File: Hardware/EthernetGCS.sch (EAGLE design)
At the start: 67 parts, among them IC3 24AA00OT, IC4 PIC24FJ64GA002_QFN, J2 HR911105A, Q2 25Mhz, U1 MIC5219-3.3V, U3 MIC5219-3.3V, U4 ENC28J60-QFN, U5 MIC5219-3.3V, U7 FT232RL-BASICSSOP, X2 USB-A-H

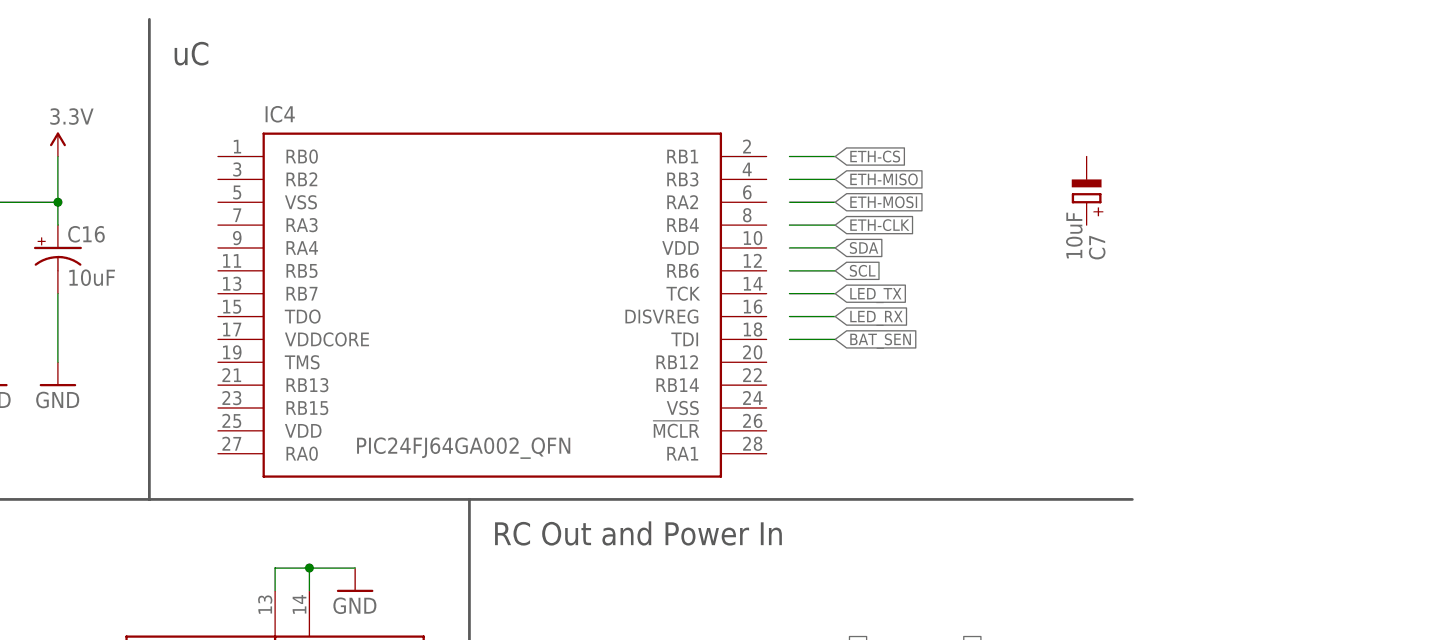
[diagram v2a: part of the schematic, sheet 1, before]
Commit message: Connecting the power pins of the uC.
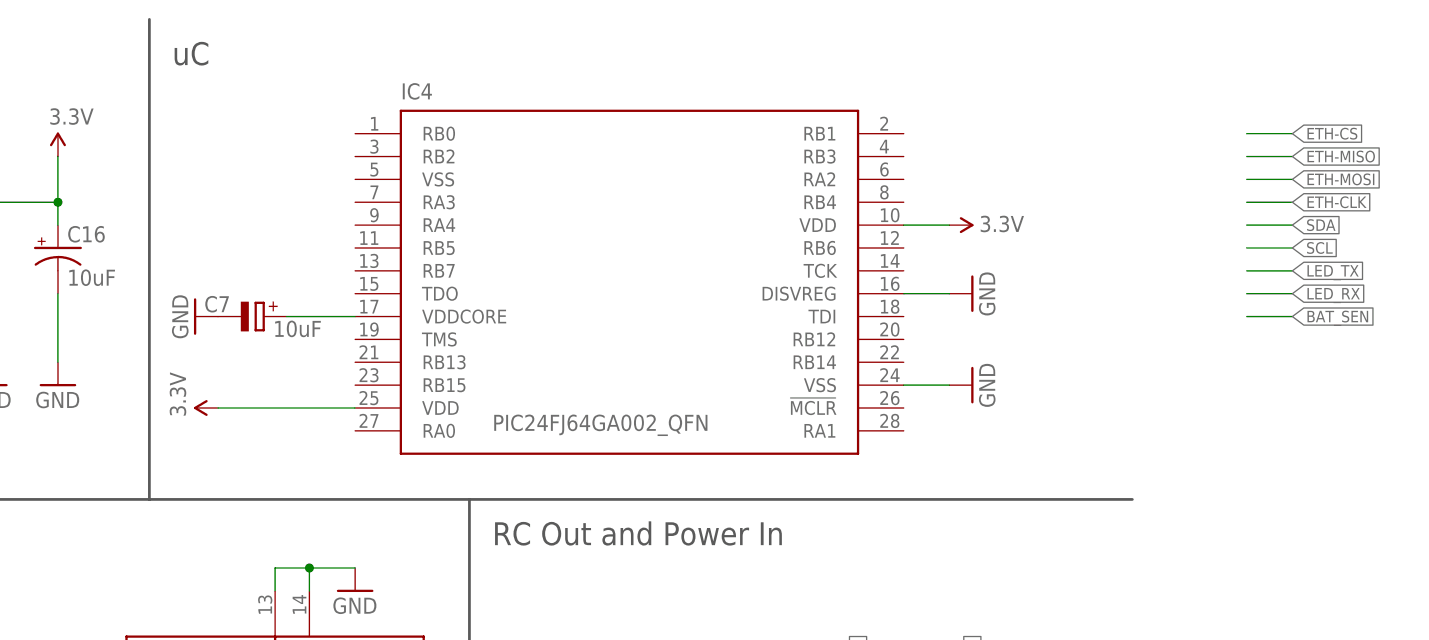
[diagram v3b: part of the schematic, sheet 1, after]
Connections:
- new net N$5: C7.+, IC4.VDDCORE
- net 3.3V: now also IC4.VDD@1, IC4.VDD@2
- net GND: now also C7.-, IC4.DISVREG, IC4.VSS@2
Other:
- moved on the sheet: C7, IC4

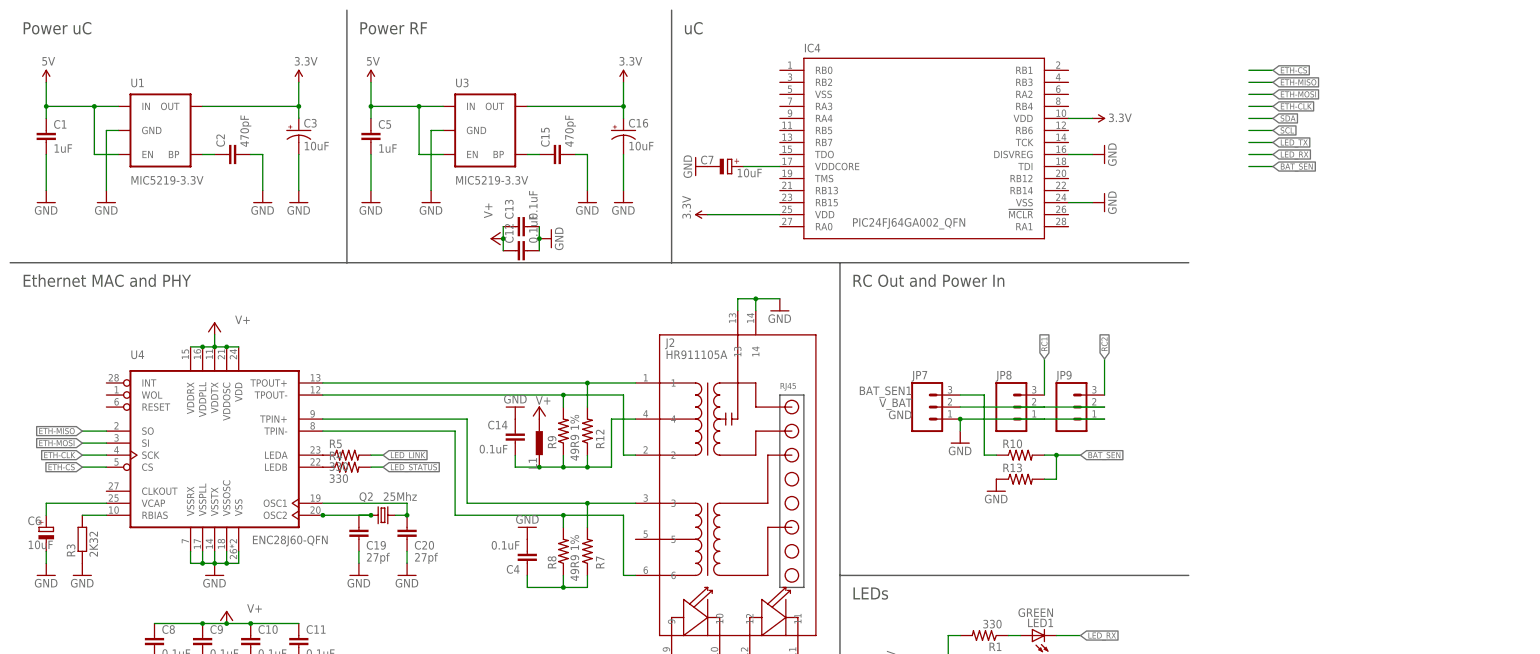
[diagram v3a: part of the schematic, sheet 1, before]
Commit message: Adding GPS port, RC output pull-ups. Connecting stuff, and changing parts positions.
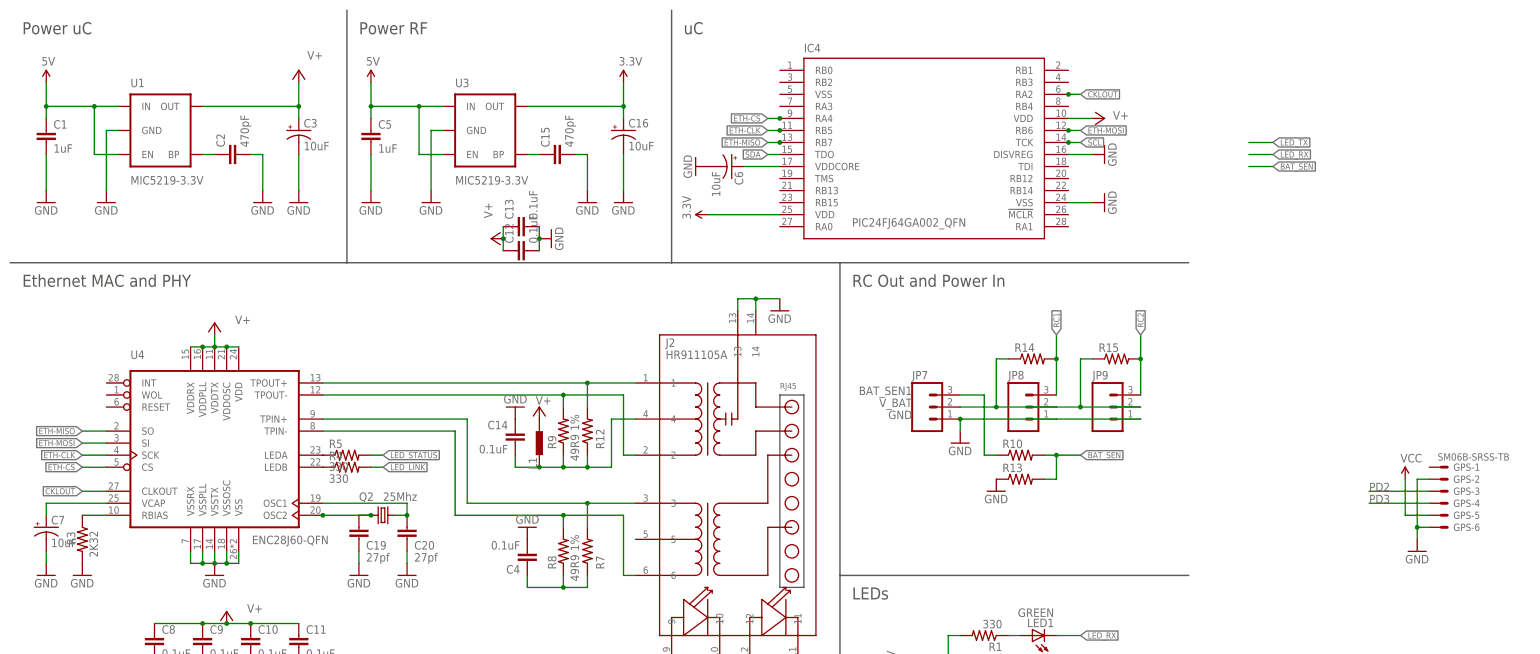
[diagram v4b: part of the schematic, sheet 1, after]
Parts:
- added GPS: SM06B-SRSS-TB, con-jst2:SM06B-SRSS-TB
- added R14, R15: (no value), SparkFun:RESISTOR0402-RES
- C6, C7: device rcl:CPOL-EUSMCA -> SparkFun:CAP_POL1206
- R3: device rcl:R-EU_R0805 -> SparkFun:RESISTOR0402-RES
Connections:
- new net CKLOUT: IC4.RA2, U4.CLKOUT
- new net PD2: GPS-3.S
- new net PD3: GPS-4.S
- new net VCC: GPS-5.S
- net 3.3V: no longer C3.+, IC4.VDD@1, U1.OUT
- net ETH-CLK: now also IC4.RB5
- net ETH-CS: now also IC4.RA4
- net ETH-MISO: now also IC4.RB7
- net ETH-MOSI: now also IC4.RB6
- net GND: now also GPS-2.S, GPS-6.S, R3.2; no longer R3.1
- net LED_LINK: now also R4.2; no longer R5.2
- net LED_STATUS: now also R5.2; no longer R4.2
- net N$13: now also C7.+; no longer C6.+
- net N$17: now also R3.1; no longer R3.2
- net N$5: now also C6.+; no longer C7.+
- net RC1: now also R14.2
- net RC2: now also R15.2
- net SCL: now also IC4.TCK
- net SDA: now also IC4.TDO
- net V+: now also C3.+, IC4.VDD@1, U1.OUT
- net V_BAT: now also R14.1, R15.1
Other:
- moved on the sheet: C6, C7, JP8, JP9

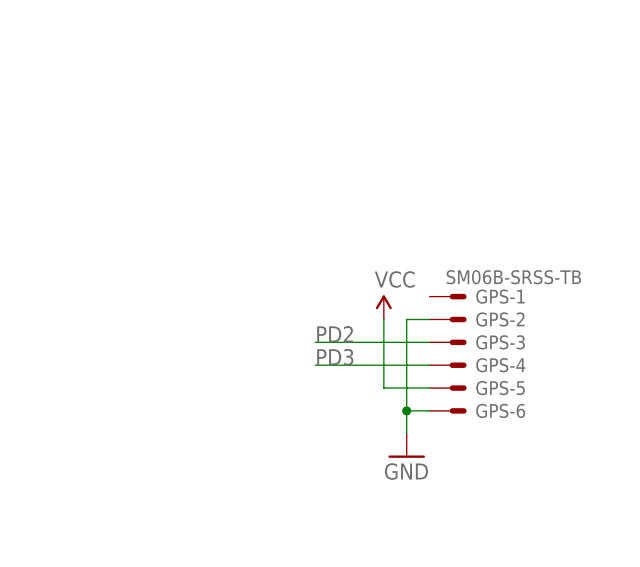
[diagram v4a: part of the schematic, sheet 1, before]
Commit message: Layout: tracing tracks.
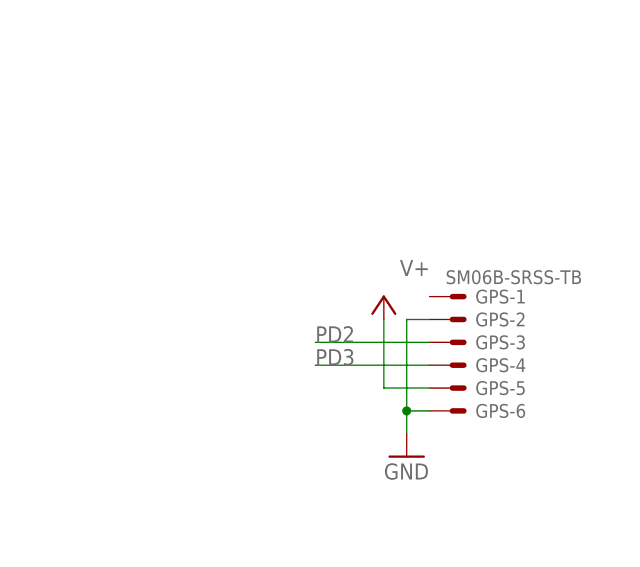
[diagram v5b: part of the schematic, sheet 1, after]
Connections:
- removed net VCC: GPS-5.S
- net V+: now also GPS-5.S
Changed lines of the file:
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@@
 <part name="GPS" library="con-jst2" deviceset="?M06B-SRSS-TB" device="S"/>
 <part name="GND44" library="supply1" deviceset="GND" device=""/>
-<part name="P+40" library="DIYdrones3" deviceset="VCC" device=""/>
+<part name="P+1" library="supply2" deviceset="V+" device=""/>
 </parts>
 <sheets>
@@
 <instance part="GPS" gate="-6" x="302.26" y="76.2"/>
 <instance part="GND44" gate="1" x="297.18" y="71.12"/>
-<instance part="P+40" gate="1" x="294.64" y="86.36"/>
+<instance part="P+1" gate="1" x="294.64" y="88.9" smashed="yes">
+<attribute name="VALUE" x="296.418" y="91.186" size="1.778" layer="96"/>
+</instance>
 </instances>
 <busses>
@@
 <pinref part="P+10" gate="1" pin="V+"/>
 </segment>
+<segment>
+<wire x1="299.72" y1="78.74" x2="294.64" y2="78.74" width="0.1524" layer="91"/>
+<wire x1="294.64" y1="78.74" x2="294.64" y2="86.36" width="0.1524" layer="91"/>
+<pinref part="GPS" gate="-5" pin="S"/>
+<pinref part="P+1" gate="1" pin="V+"/>
+</segment>
 </net>
 <net name="N$13" class="0">
@@
 </segment>
 </net>
-<net name="VCC" class="0">
-<segment>
-<wire x1="299.72" y1="78.74" x2="294.64" y2="78.74" width="0.1524" layer="91"/>
-<wire x1="294.64" y1="78.74" x2="294.64" y2="86.36" width="0.1524" layer="91"/>
-<pinref part="GPS" gate="-5" pin="S"/>
-<pinref part="P+40" gate="1" pin="VCC"/>
-</segment>
-</net>

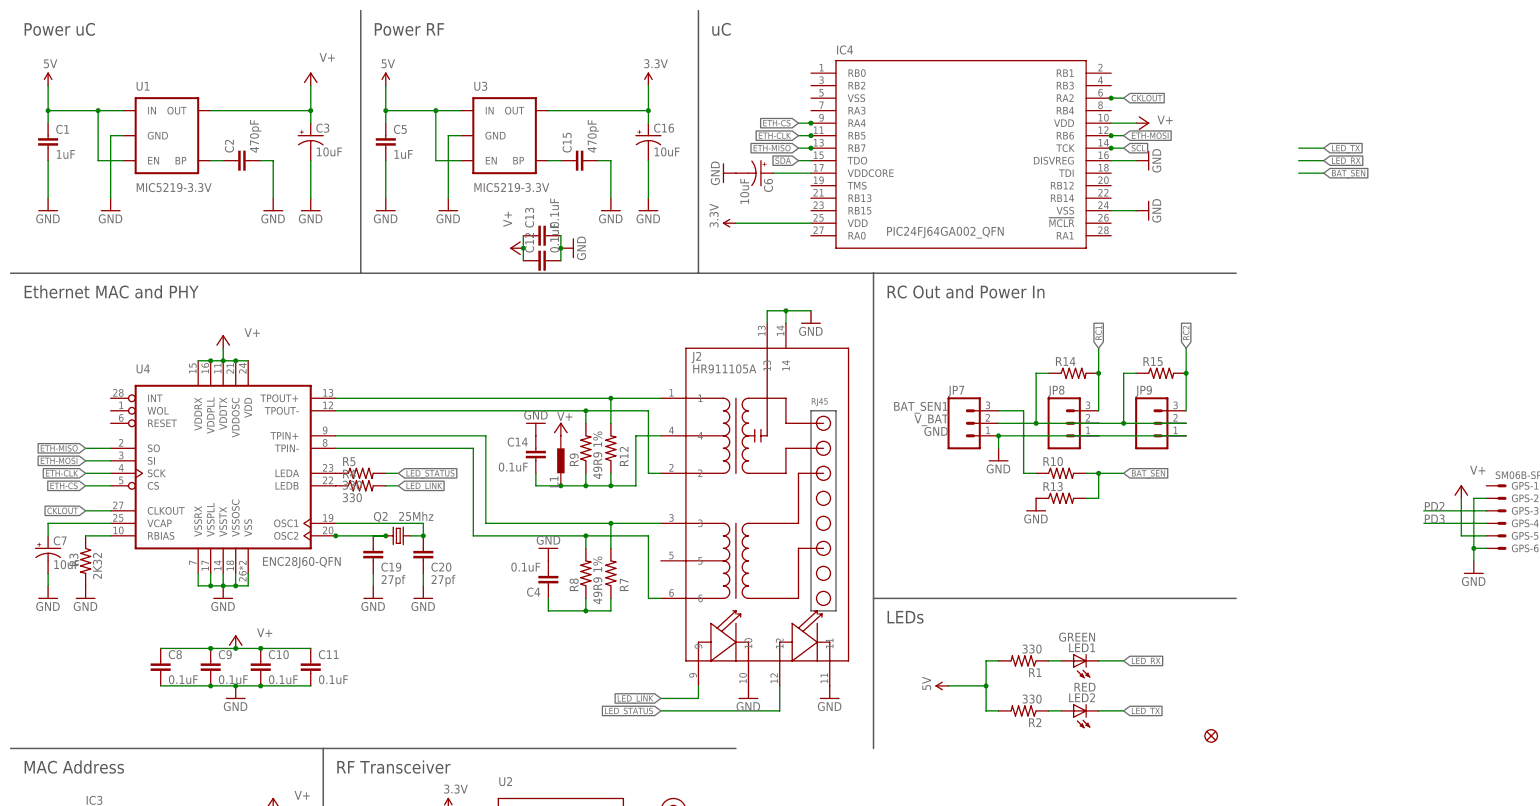
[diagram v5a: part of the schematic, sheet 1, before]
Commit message: Continuing the board layout, adding connections to the schematic
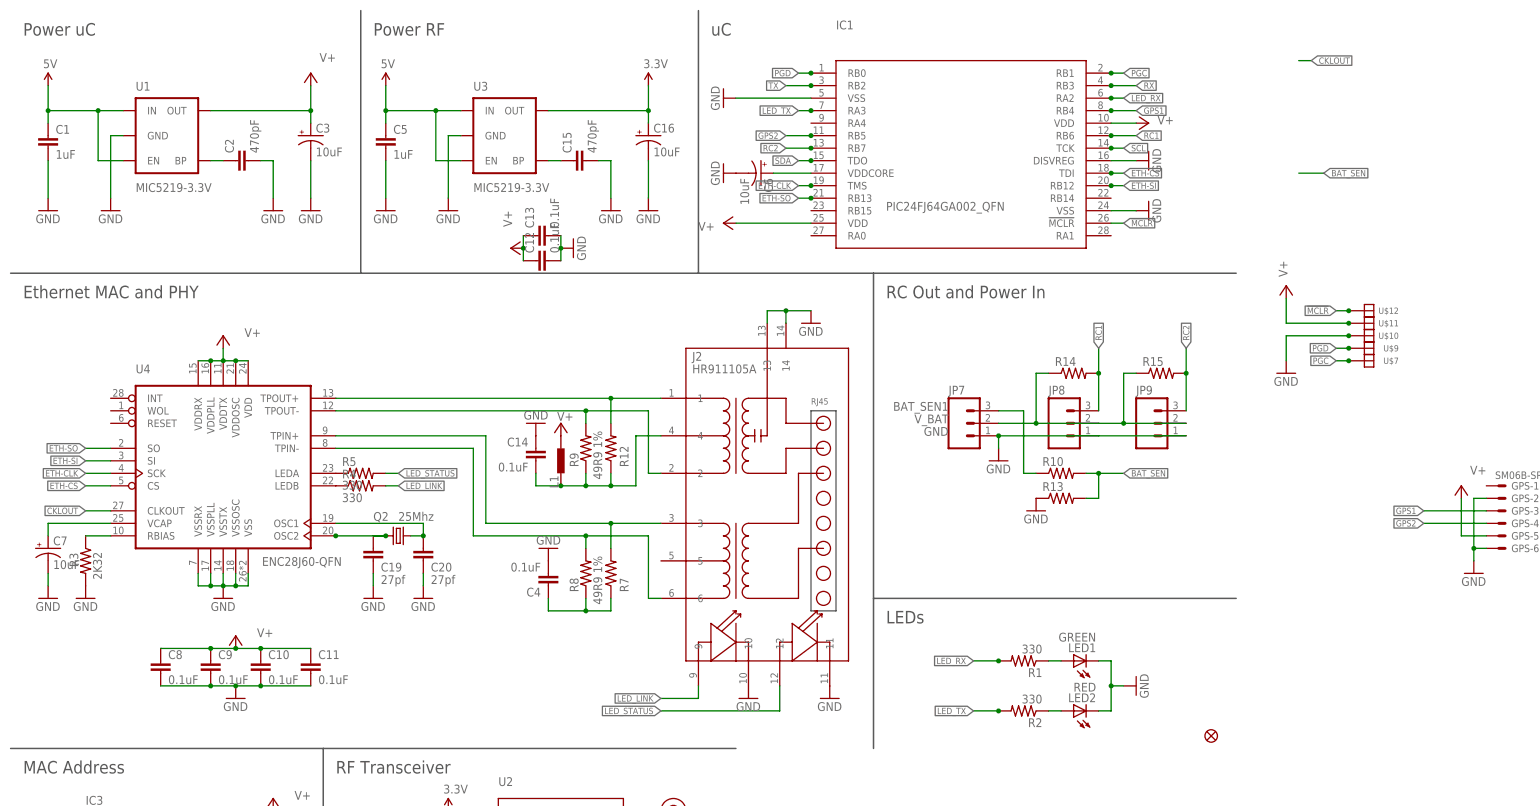
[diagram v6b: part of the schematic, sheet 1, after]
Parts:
- added U$10, U$11, U$12, U$7, U$9: SOLDER_PAD150_75, DIYdrones2:SOLDER_PAD150_75
- IC1: MPN (none) -> PIC24FJ64GA002-E/ML; OC_FARNELL (none) -> 1818728; OC_NEWARK (none) -> 98M1922
- renumbered IC4 to IC1
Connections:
- removed net ETH-MISO: IC1.RB7, U4.SO
- removed net ETH-MOSI: IC1.RB6, U4.SI
- removed net PD2: GPS-3.S
- removed net PD3: GPS-4.S
- new net !MCLR: IC1.!MCLR, U$12.P$1
- new net ETH-SI: IC1.RB12, U4.SI
- new net ETH-SO: IC1.RB13, U4.SO
- new net GPS1: GPS-3.S, IC1.RB4
- new net GPS2: GPS-4.S, IC1.RB5
- new net PGC: IC1.RB1, U$7.P$1
- new net PGD: IC1.RB0, U$9.P$1
- net 3.3V: no longer IC1.VDD@2
- net 5V: no longer R1.2, R2.2
- net CKLOUT: no longer IC1.RA2
- net ETH-CLK: now also IC1.TMS; no longer IC1.RB5
- net ETH-CS: now also IC1.TDI; no longer IC1.RA4
- net GND: now also IC1.VSS@1, LED1.C, LED2.C, U$10.P$1
- net LED_RX: now also IC1.RA2, R1.2; no longer LED1.C
- net LED_TX: now also IC1.RA3, R2.2; no longer LED2.C
- net RC1: now also IC1.RB6
- net RC2: now also IC1.RB7
- net RX: now also IC1.RB3
- net TX: now also IC1.RB2
- net V+: now also IC1.VDD@2, U$11.P$1

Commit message: More Layout, and designing the power section of the board
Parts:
- added D1: MBR120VLSFT1G, adafruit:DIODESOD-123
- added D4: MMSZ5233BT1G, adafruit:DIODESOD-123
- added F2: 500mA, SparkFun:PTCSMD
- added JP1: (no value), SparkFun-Connectors:M03PTH
- added SJ1: (no value), SparkFun:SOLDERJUMPER_2WAYT
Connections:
- removed net BAT_SEN1: JP7.3, R10.1
- removed net V_BAT: JP7.2, JP8.2, JP9.2, R14.1, R15.1
- new net N$10: JP7.3, SJ1.3
- new net N$11: JP1.2, R10.1
- new net N$6: D1.C, F2.1
- new net V_IN: D1.A, SJ1.2
- new net V_RC: JP7.2, JP8.2, JP9.2, R14.1, R15.1, SJ1.1
- net 5V: now also D4.C, F2.2
- net BAT_SEN: now also IC1.RB14
- net CTS: now also IC1.RA4
- net GND: now also D4.A, JP1.1
- net RTS: now also IC1.RA1
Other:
- moved on the sheet: GPS-1, GPS-2, GPS-3, GPS-4, GPS-5, GPS-6, JP7, R10, R13, U$10, U$11, U$12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

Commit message: More Layout...
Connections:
- net 5V: now also GPS-5.S
- net V+: no longer GPS-5.S
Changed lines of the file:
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@@
 <part name="GPS" library="con-jst2" deviceset="?M06B-SRSS-TB" device="S"/>
 <part name="GND44" library="supply1" deviceset="GND" device=""/>
-<part name="P+1" library="supply2" deviceset="V+" device=""/>
 <part name="IC1" library="microchip" deviceset="PIC24FJ64GA002_QFN" device="">
 <attribute name="MF" value=""/>
@@
 <part name="SJ1" library="SparkFun" deviceset="SOLDERJUMPER_2WAY" device="T"/>
 <part name="GND48" library="supply1" deviceset="GND" device=""/>
+<part name="U$8" library="SparkFun" deviceset="5V" device=""/>
 </parts>
 <sheets>
@@
 <instance part="GPS" gate="-6" x="309.88" y="160.02"/>
 <instance part="GND44" gate="1" x="304.8" y="154.94"/>
-<instance part="P+1" gate="1" x="302.26" y="172.72" smashed="yes">
-<attribute name="VALUE" x="304.038" y="175.006" size="1.778" layer="96"/>
-</instance>
 <instance part="IC1" gate="G$1" x="193.04" y="157.48" smashed="yes">
 <attribute name="NAME" x="167.64" y="181.61" size="1.778" layer="95" font="vector"/>
@@
 </instance>
 <instance part="GND48" gate="1" x="279.4" y="66.04"/>
+<instance part="U$8" gate="G$1" x="302.26" y="170.18"/>
 </instances>
 <busses>
@@
 <wire x1="332.74" y1="104.14" x2="350.52" y2="104.14" width="0.1524" layer="91"/>
 </segment>
+<segment>
+<wire x1="307.34" y1="162.56" x2="302.26" y2="162.56" width="0.1524" layer="91"/>
+<wire x1="302.26" y1="162.56" x2="302.26" y2="170.18" width="0.1524" layer="91"/>
+<pinref part="GPS" gate="-5" pin="S"/>
+<pinref part="U$8" gate="G$1" pin="5V"/>
+</segment>
 </net>
 <net name="3.3V" class="0">
@@
 </segment>
 <segment>
-<wire x1="307.34" y1="162.56" x2="302.26" y2="162.56" width="0.1524" layer="91"/>
-<wire x1="302.26" y1="162.56" x2="302.26" y2="170.18" width="0.1524" layer="91"/>
-<pinref part="GPS" gate="-5" pin="S"/>
-<pinref part="P+1" gate="1" pin="V+"/>
-</segment>
-<segment>
